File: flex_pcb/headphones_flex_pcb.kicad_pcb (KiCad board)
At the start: 2 copper layers, 42 x 25 mm, 14 parts, among them J1 LIGHTING_JACK, J3 BOTTOM_FLEX_LIGHTNING, J5 LIGHTNING_HEADPHONE_ADAPTER, J7 IPHONE_HEADPHONE_JACK, J8 CONN_01X02, U1 SN74LVC1G123, U2 ADG774A-LFCSP, U3 SN74LVC1G123, U4 NC7S32-micropak6

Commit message: About to try front fold
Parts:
- removed J8: CONN_01X02, Pin_Headers:Pin_Header_Straight_1x02_Pitch2.54mm
- added J2: CONN_01X01, wire_pads:WIRE_PAD_2x3mm, F.Cu at (145.2, 73.1)
- C1, C2, R1, R2, R3: moved to F.Cu
- J3: footprint lightning_flex_pads:LIGHTNING_FLEX_PADS -> lightning_flex_pads:LIGHTNING_FLEX_PADS_NO_CRTYD
- U1, U2, U3: moved to B.Cu
- moved U4 12.7 mm to (134.4, 81.5)
- moved C1 10.9 mm to (133.8, 77.9), turned to 90 degrees
- moved U1 9.96 mm to (134.6, 77.8), turned to 270 degrees
- moved R1 9.53 mm to (135.2, 77.8), turned to 90 degrees
- moved C2 8.70 mm to (134.0, 82.1)
- moved R2 8.60 mm to (133.8, 79.8), turned to 270 degrees
- moved R3 8.52 mm to (134.9, 80.0), turned to 270 degrees
- moved U3 7.78 mm to (134.4, 79.8), turned to 90 degrees
- moved U2 7.36 mm to (135.9, 74.7)
- moved J5 2.86 mm to (136.9, 66.9)
- moved J7 0.71 mm to (122.7, 72.3)
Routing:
- net /JPIN2: track 34.7 -> 0.00 mm
- net /JPIN3: track 32.2 -> 0.00 mm
- net Net-(J1-Pad1): track 32.5 -> 10.4 mm, vias 2 -> 0
- net /PSHIELD: track 34.1 -> 14.2 mm, vias 2 -> 0
- net /PPIN4: track 33.5 -> 13.7 mm
- net /JPIN4: track 30.3 -> 11.0 mm
- net /PPIN6: track 27.8 -> 9.35 mm
- net /PPIN8: track 25.2 -> 6.85 mm
- net /PPIN2: track 35.2 -> 17.6 mm
- net Net-(J5-Pad14): track 23.9 -> 6.33 mm, vias 1 -> 0
- net /PPIN5: track 29.4 -> 12.9 mm
- net /PPIN7: track 26.5 -> 10.5 mm
- net /PPIN3: track 31.1 -> 15.6 mm
- net Net-(J5-Pad15): track 21.2 -> 5.74 mm
- net GNDREF: track 5.53 -> 19.4 mm
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- removed copper zone on F.Cu, net GNDREF
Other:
- board size 42 x 25 mm -> 42 x 24.2 mm
- board text added: "Add tabs from this side instead"
- board text added: "V0.7"
- board text added: "v0.7"

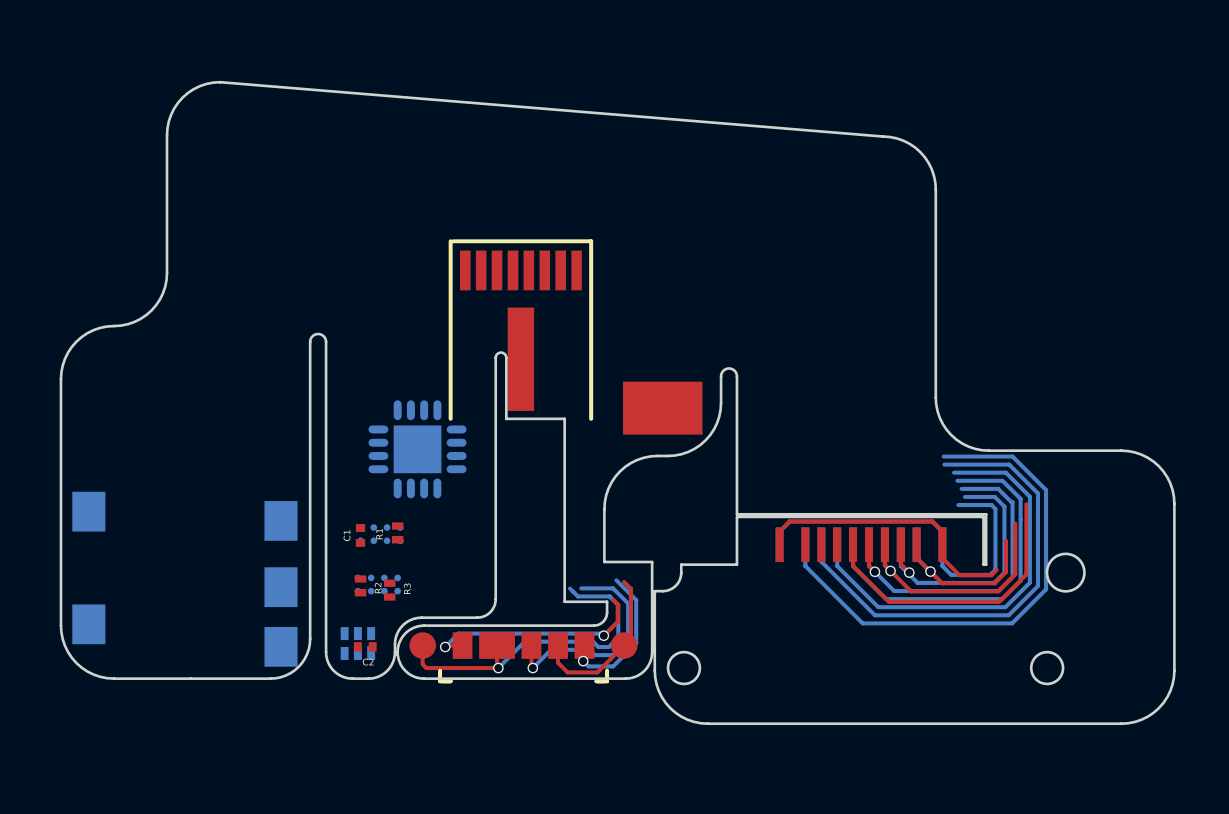
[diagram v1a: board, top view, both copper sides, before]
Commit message: WIP: just before switching from 0201 -> 0402
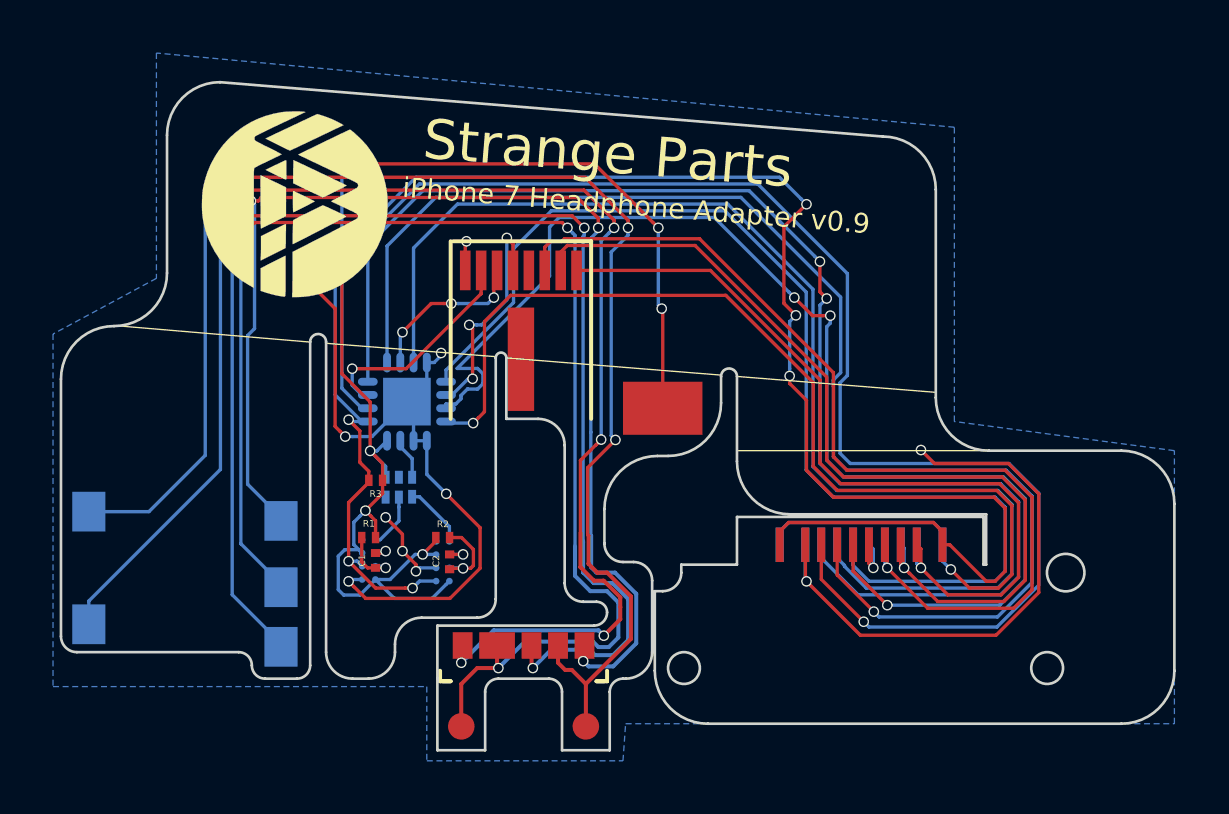
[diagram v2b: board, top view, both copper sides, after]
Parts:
- added G***: LOGO, strange_parts_logo:strange_parts_logo-7mm, F.Cu at (131.3, 65.4)
- J5: footprint lightning_headphone_adapter:LIGHTNING_HEADPHONE_ADAPTER -> lightning_headphone_adapter:LIGHTNING_HEADPHONE_ADAPTER_FRONT_FOLD
- U2: value ADG774A-LFCSP -> SN74LVC1G123; footprint Housings_DFN_QFN:QFN-16-1EP_3x3mm_Pitch0.5mm -> DSBGA-8:DSBGA-8_2x4_0.9x1.9mm_Pitch0.5mm_Dia0.25mm
- U3: value SN74LVC1G123 -> NC7S32-micropak6; footprint DSBGA-8:DSBGA-8_2x4_0.9x1.9mm_Pitch0.5mm_Dia0.25mm -> micropak6:Micropak6
- U4: value NC7S32-micropak6 -> ADG774A-LFCSP; footprint micropak6:Micropak6 -> Housings_DFN_QFN:QFN-16-1EP_3x3mm_Pitch0.5mm
- moved U4 8.70 mm to (135.6, 72.8), turned to 0 degrees
- moved C2 4.52 mm to (137.2, 78.9), turned to 90 degrees
- moved U3 4.44 mm to (136.0, 75.6), turned to 180 degrees
- moved U2 4.33 mm to (136.9, 78.9), turned to 0 degrees
- moved R3 4.17 mm to (134.4, 75.8), turned to 180 degrees
- moved R2 3.60 mm to (136.9, 78.0), turned to 0 degrees
- moved R1 1.11 mm to (134.1, 78.0), turned to 180 degrees
- moved C1 1.10 mm to (134.4, 78.8)
- moved U1 1.06 mm to (134.1, 78.8), turned to 0 degrees
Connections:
- J1 pad 1: Net-(J1-Pad1) -> /JSHIELD
- J1 pad 10: Net-(J1-Pad1) -> /JSHIELD
- R3 pad 2: Net-(J1-Pad1) -> /JSHIELD
- U1 pad 2: Net-(J1-Pad1) -> /JSHIELD
- U2 pad 1: Net-(J1-Pad1) -> /JSHIELD
- U2 pad 2: /JPIN2 -> GNDREF
- U2 pad 3: /HPIN2 -> VCC
- U2 pad 4: /PPIN2 -> GNDREF
- U2 pad 5: /JPIN3 -> Net-(U2-Pad5)
- U2 pad 6: /HPIN3 -> Net-(C2-Pad2)
- U2 pad 7: /PPIN3 -> Net-(C2-Pad1)
- U2 pad 8: GNDREF -> VCC
- U3 pad 1: Net-(J1-Pad1) -> Net-(U2-Pad5)
- U3 pad 2: GNDREF -> Net-(U1-Pad5)
- U3 pad 3: VCC -> GNDREF
- U3 pad 4: GNDREF -> Net-(U3-Pad4)
- U3 pad 5: Net-(U3-Pad5) -> (no net)
- U3 pad 6: Net-(C2-Pad2) -> VCC
- U4 pad 1: Net-(U3-Pad5) -> /JSHIELD
- U4 pad 2: Net-(U1-Pad5) -> /JPIN2
- U4 pad 3: GNDREF -> /HPIN2
- U4 pad 4: Net-(U2-Pad15) -> /PPIN2
- U4 pad 5: (no net) -> /JPIN3
- U4 pad 6: VCC -> /HPIN3
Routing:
- net /JSHIELD: track 0.00 -> 69.3 mm, vias 0 -> 6
- net /JPIN2: track 0.00 -> 57.1 mm, vias 0 -> 1
- net Net-(J5-Pad14): track 6.33 -> 58.3 mm, vias 0 -> 3
- net /JPIN3: track 0.00 -> 51.1 mm, vias 0 -> 1
- net VCC: track 0.00 -> 49.9 mm, vias 0 -> 7
- net Net-(J5-Pad11): track 8.53 -> 55.0 mm, vias 2 -> 5
- net Net-(J5-Pad12): track 13.0 -> 54.9 mm, vias 1 -> 3
- net Net-(J5-Pad13): track 8.45 -> 49.7 mm, vias 1 -> 3
- net Net-(J5-Pad15): track 5.74 -> 46.6 mm, vias 1 -> 3
- net /JPIN4: track 11.0 -> 47.5 mm, vias 0 -> 3
- net /PPIN2: track 17.6 -> 51.7 mm, vias 0 -> 2
- net GNDREF: track 19.4 -> 50.9 mm, vias 0 -> 11
- net /PPIN3: track 15.6 -> 46.6 mm
- net /PSHIELD: track 14.2 -> 44.4 mm, vias 0 -> 2
- net /PPIN4: track 13.7 -> 43.1 mm
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- added copper zone on B.Cu, net GNDREF
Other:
- board size 42 x 24.2 mm -> 42 x 25.2 mm
- net class Default: clearance 0.1524 -> 0.126; trace_width 0.1524 -> 0.127
- rule trace_clearance: 0.1524 -> 0.126
- rule trace_min: 0.1524 -> 0.127
- board text added: "Strange Parts"
- board text added: "iPhone 7 Headphone Adapter v0.9"
- board text removed: "Add tabs from this side instead"
- board text removed: "TODOS: - Check to see if adapter actually needs top two headphone wire pads connected - change footprint of adapter to have proper foldover tabs - check alignment of everything - Figure out how power is going to attach"
- board text removed: "V0.7"
- board text removed: "v0.7"

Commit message: First flex pcb version - ready to fab. v0.9
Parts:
- C1, C2: footprint Capacitors_SMD:C_0201_NoSilk -> Capacitors_SMD:C_0402_NoSilk
- R1, R2, R3: footprint Resistors_SMD:R_0201_NoSilk -> Resistors_SMD:R_0402_NoSilk
- moved R1 0.40 mm to (134.2, 77.6)
- moved R2 0.38 mm to (136.9, 77.6)
- moved C1 0.22 mm to (134.4, 79.1)
- moved C2 0.14 mm to (137.2, 79.0)
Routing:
- net VCC: track 49.9 -> 51.7 mm
- net Net-(C1-Pad1): track 2.33 -> 3.73 mm
- net GNDREF: track 50.9 -> 52.3 mm

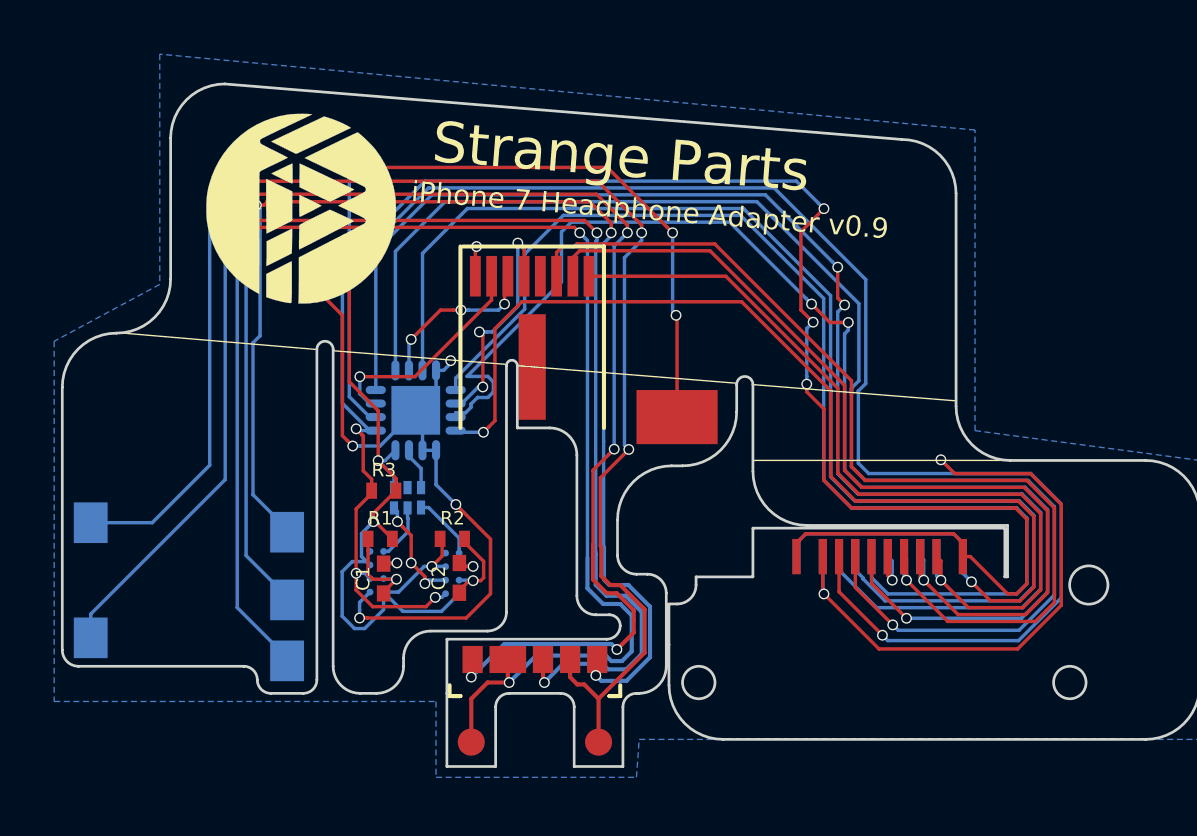
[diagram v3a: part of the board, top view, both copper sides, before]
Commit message: Switch to using iphone 5 headphone jack
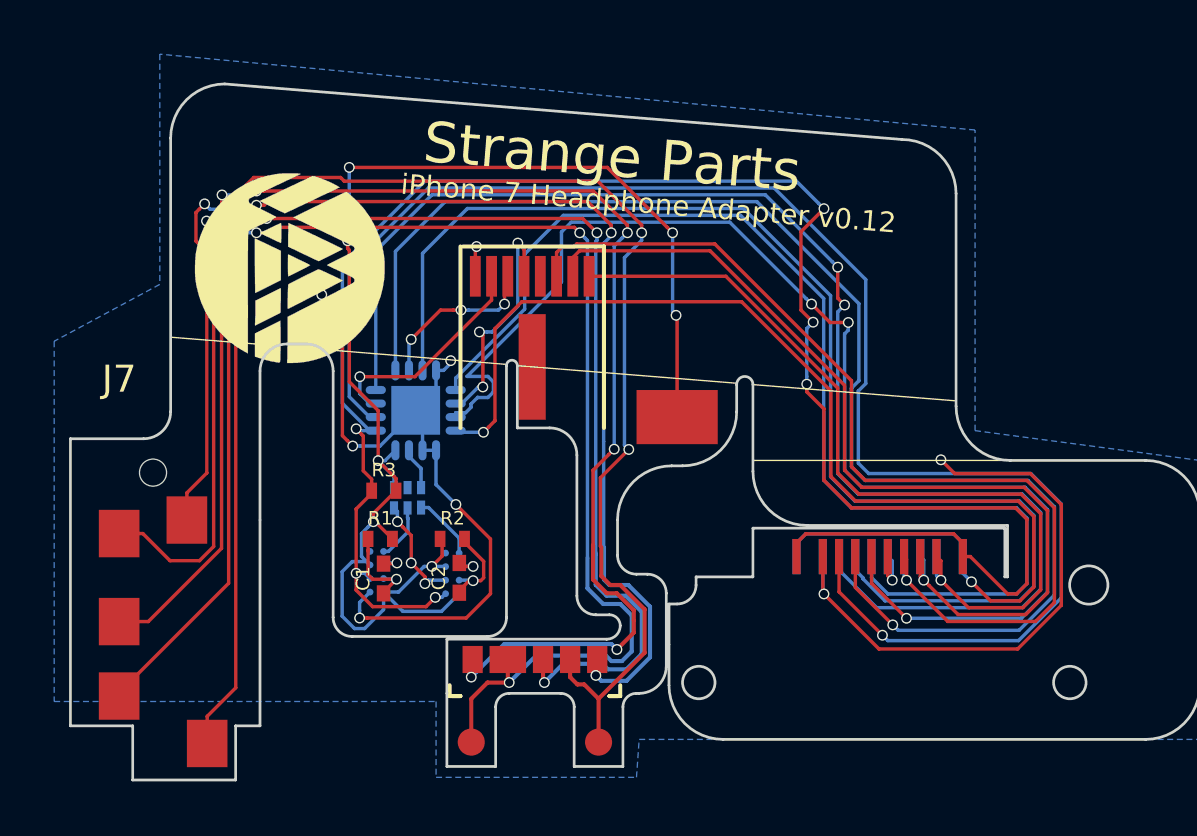
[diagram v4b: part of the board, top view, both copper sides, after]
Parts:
- J7: footprint iphone_6s_headphone_jack:IPHONE_6S_HEADPHONE_JACK -> iphone_5_headphone_jack:IPHONE_5_HEADPHONE_JACK; moved to F.Cu
- moved J7 11.2 mm to (124.6, 83.4), turned to 180 degrees
- moved G*** 2.23 mm to (130.9, 67.6)
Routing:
- net Net-(J5-Pad12): track 54.9 -> 58.0 mm, vias 3 -> 4
- net Net-(J5-Pad13): track 49.7 -> 52.7 mm, vias 3 -> 4
- net Net-(J5-Pad11): track 55.0 -> 57.6 mm, vias 5 -> 6
- net Net-(J5-Pad14): track 58.3 -> 60.1 mm, vias 3 -> 2
- net Net-(J5-Pad15): track 46.6 -> 48.1 mm, vias 3 -> 4
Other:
- board size 42 x 25.2 mm -> 41.7 x 25.7 mm
- board text added: "iPhone 7 Headphone Adapter v0.12"
- board text removed: "iPhone 7 Headphone Adapter v0.9"

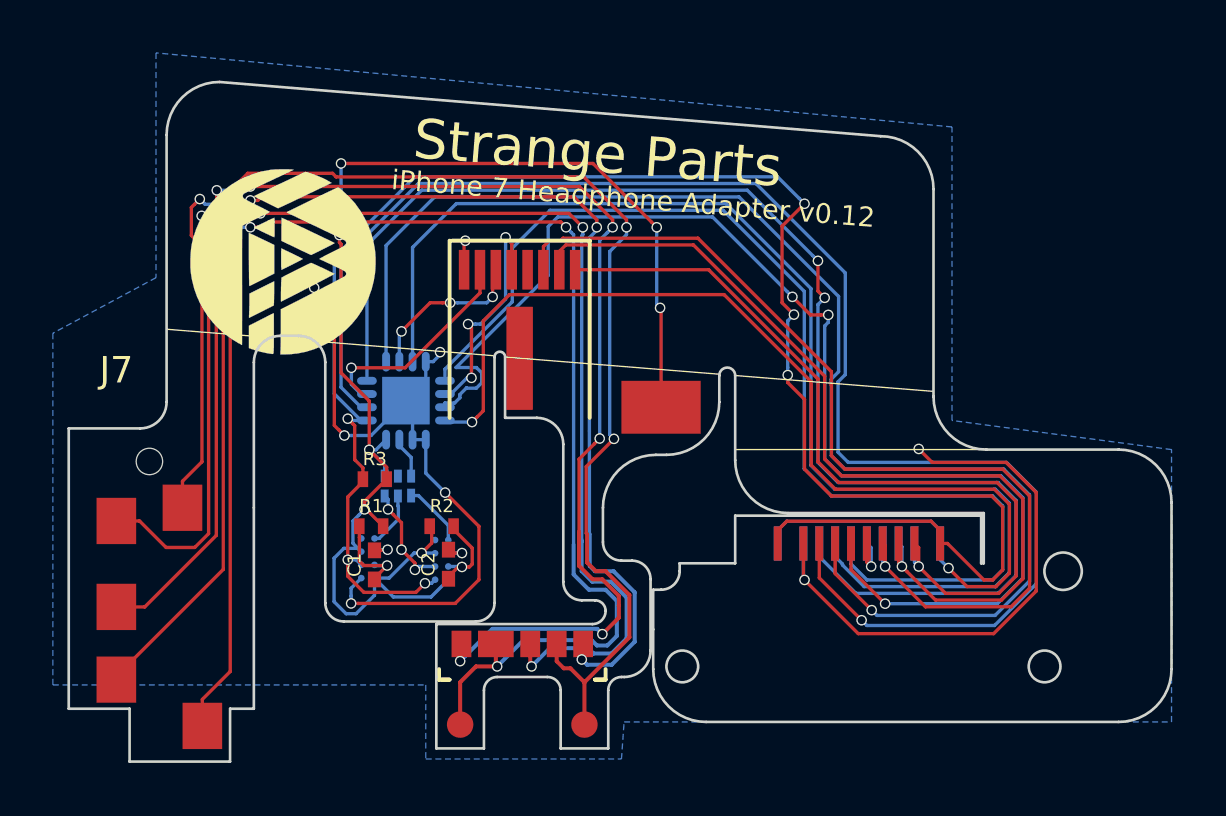
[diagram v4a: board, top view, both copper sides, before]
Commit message: Switch headphone adapter to handwired
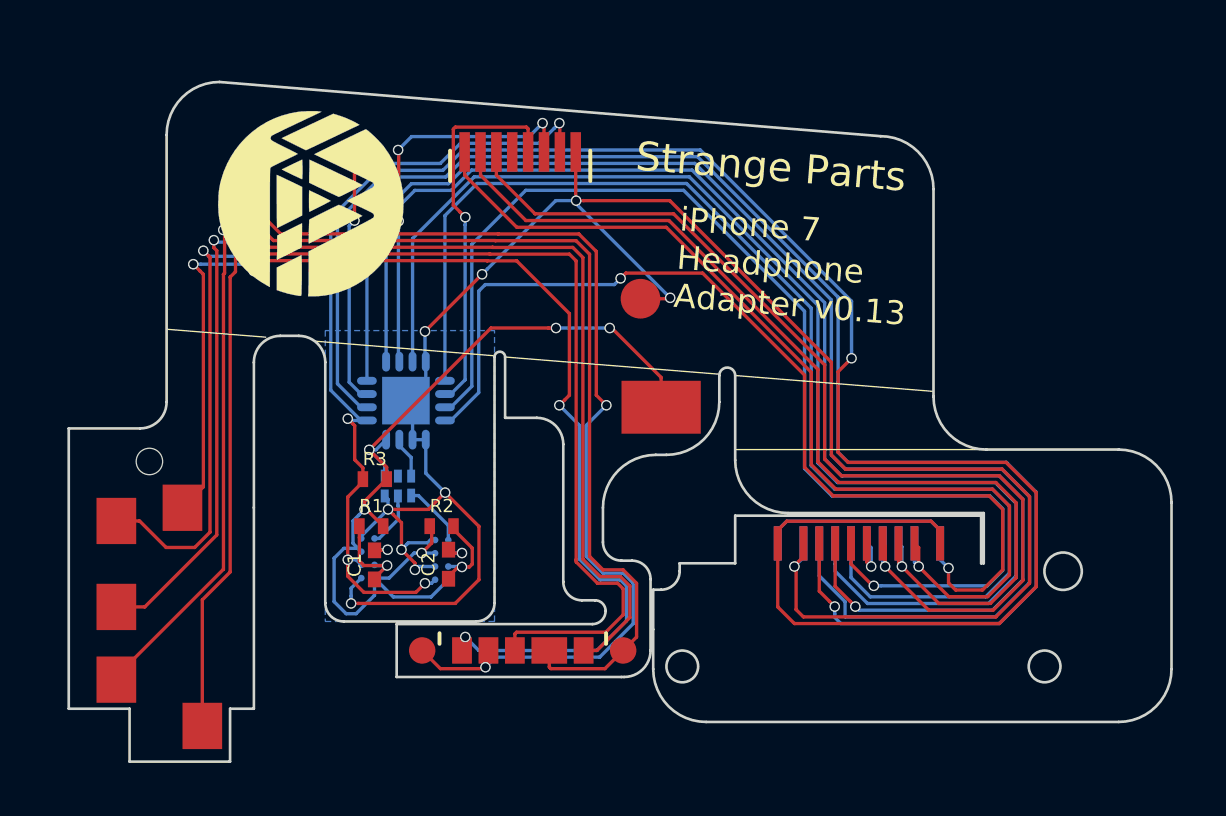
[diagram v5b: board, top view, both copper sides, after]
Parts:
- J5: footprint lightning_headphone_adapter:LIGHTNING_HEADPHONE_ADAPTER_FRONT_FOLD -> lightning_headphone_adapter:LIGHTNING_HEADPHONE_ADAPTER_HANDWIRE
- moved G*** 2.43 mm to (132.0, 65.4)
- moved J5 2.25 mm to (136.9, 64.6)
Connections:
- J5 pad 1: (no net) -> GNDREF
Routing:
- net GNDREF: track 52.3 -> 85.6 mm, vias 11 -> 10
- net VCC: track 51.7 -> 35.4 mm, vias 7 -> 5
- net /JSHIELD: track 69.7 -> 81.0 mm, vias 6 -> 4
- net /HPIN2: track 8.28 -> 18.6 mm, vias 1 -> 3
- net Net-(J5-Pad11): track 57.6 -> 47.4 mm, vias 6 -> 2
- net /HPIN3: track 6.24 -> 15.0 mm
- net /PPIN8: track 31.2 -> 37.4 mm
- net /HPIN4: track 8.81 -> 14.4 mm, vias 3 -> 1
- net Net-(J5-Pad12): track 58.0 -> 53.1 mm, vias 4 -> 2
- net /PPIN4: track 43.1 -> 47.1 mm
- net Net-(J5-Pad13): track 52.7 -> 48.9 mm, vias 4 -> 2
- net /PPIN7: track 34.4 -> 38.3 mm
- net /PPIN2: track 51.7 -> 54.4 mm, vias 2 -> 0
- net Net-(J5-Pad15): track 48.1 -> 45.6 mm
- net /PPIN6: track 37.1 -> 39.2 mm
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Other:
- outline, holes or cut-outs redrawn
- board text added: "iPhone 7 Headphone Adapter v0.13"
- board text removed: "iPhone 7 Headphone Adapter v0.12"
